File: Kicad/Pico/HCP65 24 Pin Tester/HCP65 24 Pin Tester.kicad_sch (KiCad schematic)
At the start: 64 parts, among them IC1 SN74ABT245BDBR, IC2 SN74ABT245BDBR, IC3 SN74ABT245BDBR, J1 6339167-2, J3 Conn_01x12_Socket, J8 Conn_01x12_Socket, J9 Conn_01x12_Socket

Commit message: Added debug points to Tester boards.
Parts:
- added C10: 10μF, SamacSys_Parts:CP_Radial_D4.0mm_P2.00mm, symbol HCP65:C_Radial_D4.0mm_P2.00mm
- added H1, H2, H3, H4, H5, H6, H7, H8: MountingHole_Pad, MountingHole:MountingHole_3.2mm_M3_Pad, symbol Mechanical:MountingHole_Pad
- added LED49: 150224SS73100, SamacSys_Parts:150224SS73100A, symbol Wurth_Elektronik:150224SS73100
- added R12: 10KΩ, SamacSys_Parts:R_0805, symbol HCP65:R_0805
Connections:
- net 12V: now also H1.1
- net 5V_{1} renamed 5Vc
- net 5Vc: now also H4.1
- net 5V_{2} renamed 5Vb
- net 5Vb: now also H3.1
- net 5V_{3} renamed 5Va
- net 5Va: now also C10.1, H2.1, R12.1
- net GND_{1} renamed GNDd
- net GNDd: now also H8.1
- net GND_{2} renamed GNDc
- net GNDc: now also H6.1
- net GND_{3} renamed GNDb
- net GNDb: now also C10.2, H7.1, LED49.1
- net GND_{4} renamed GNDa
- net GNDa: now also H5.1
- new net: LED49.2, R12.2
- no-connect marks 7 -> 5

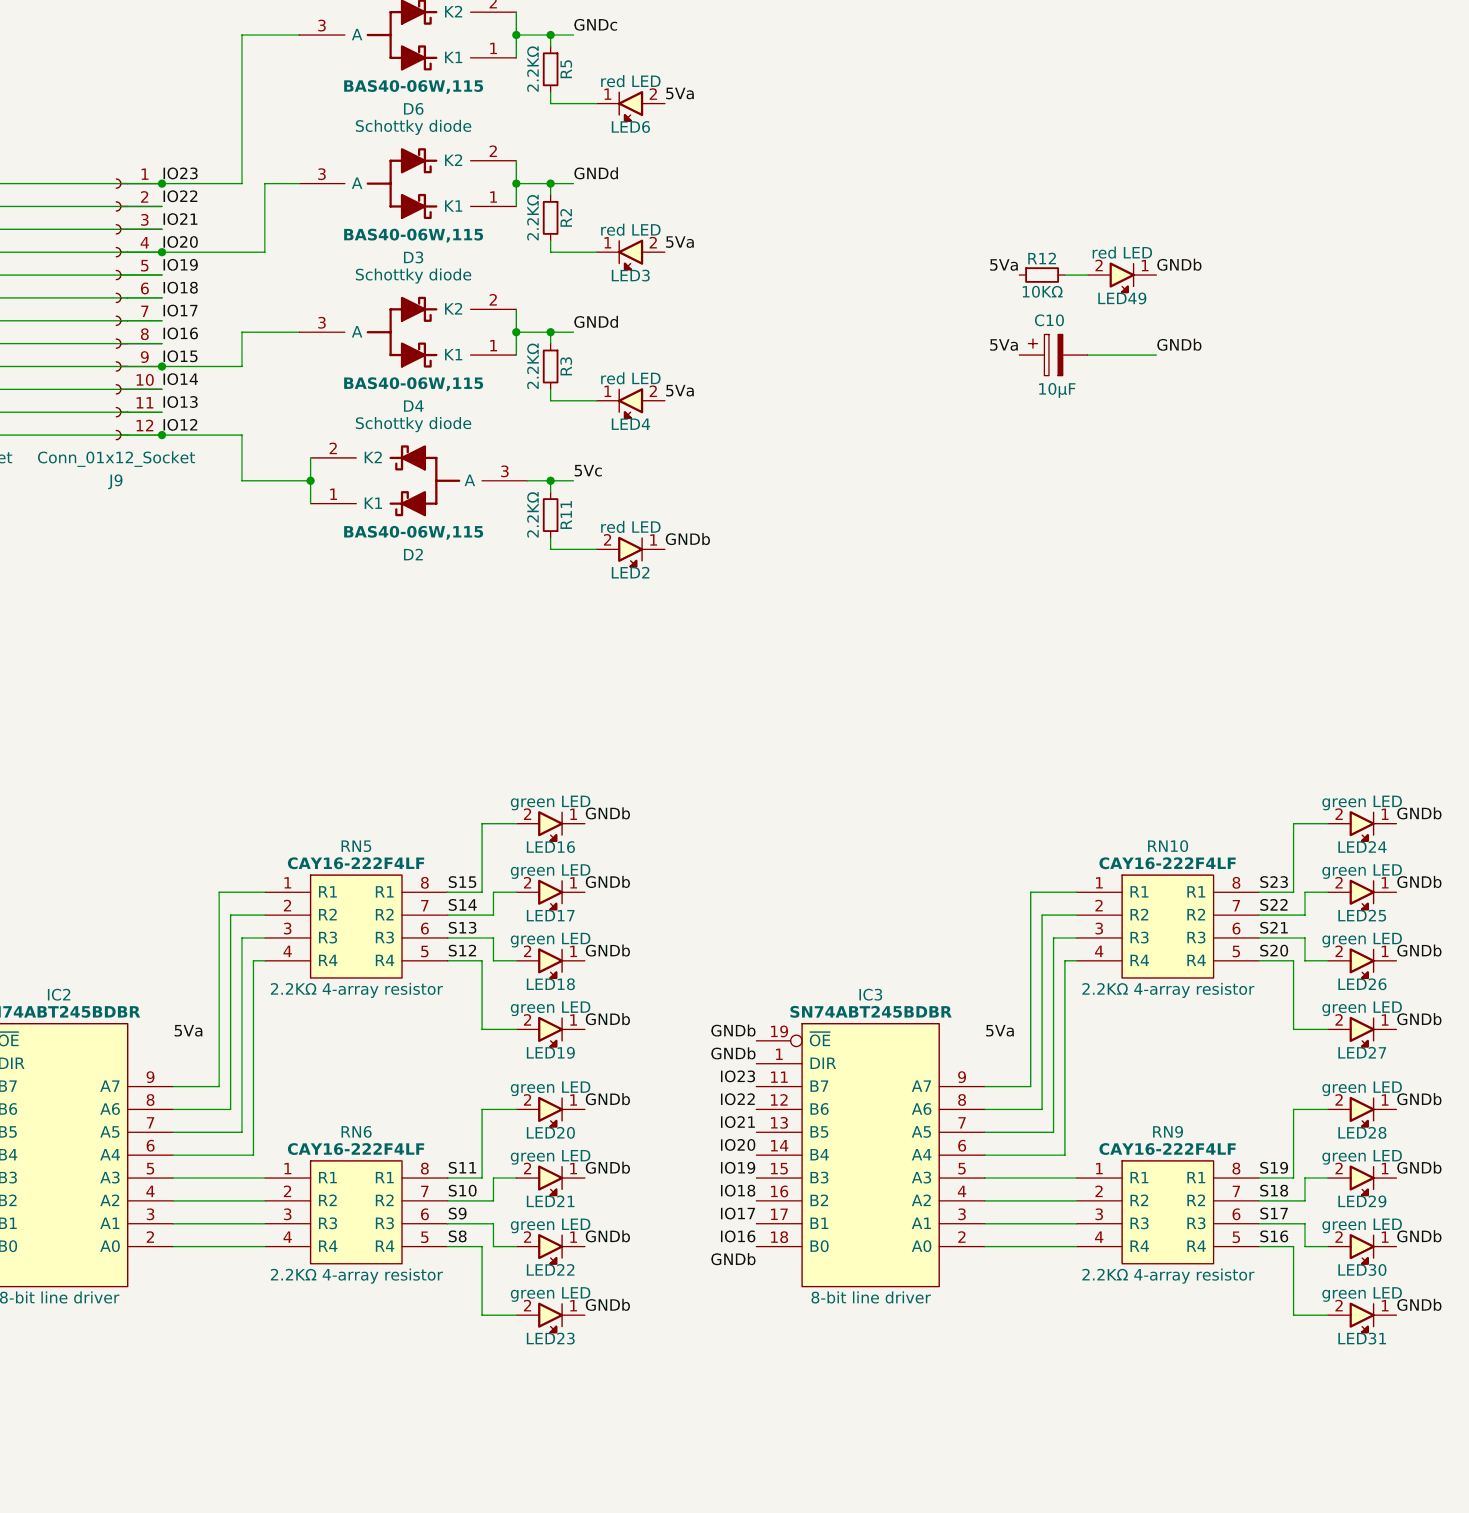
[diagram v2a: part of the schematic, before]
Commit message: Started fixing 24, 32 and 40 pin Tester Boards.
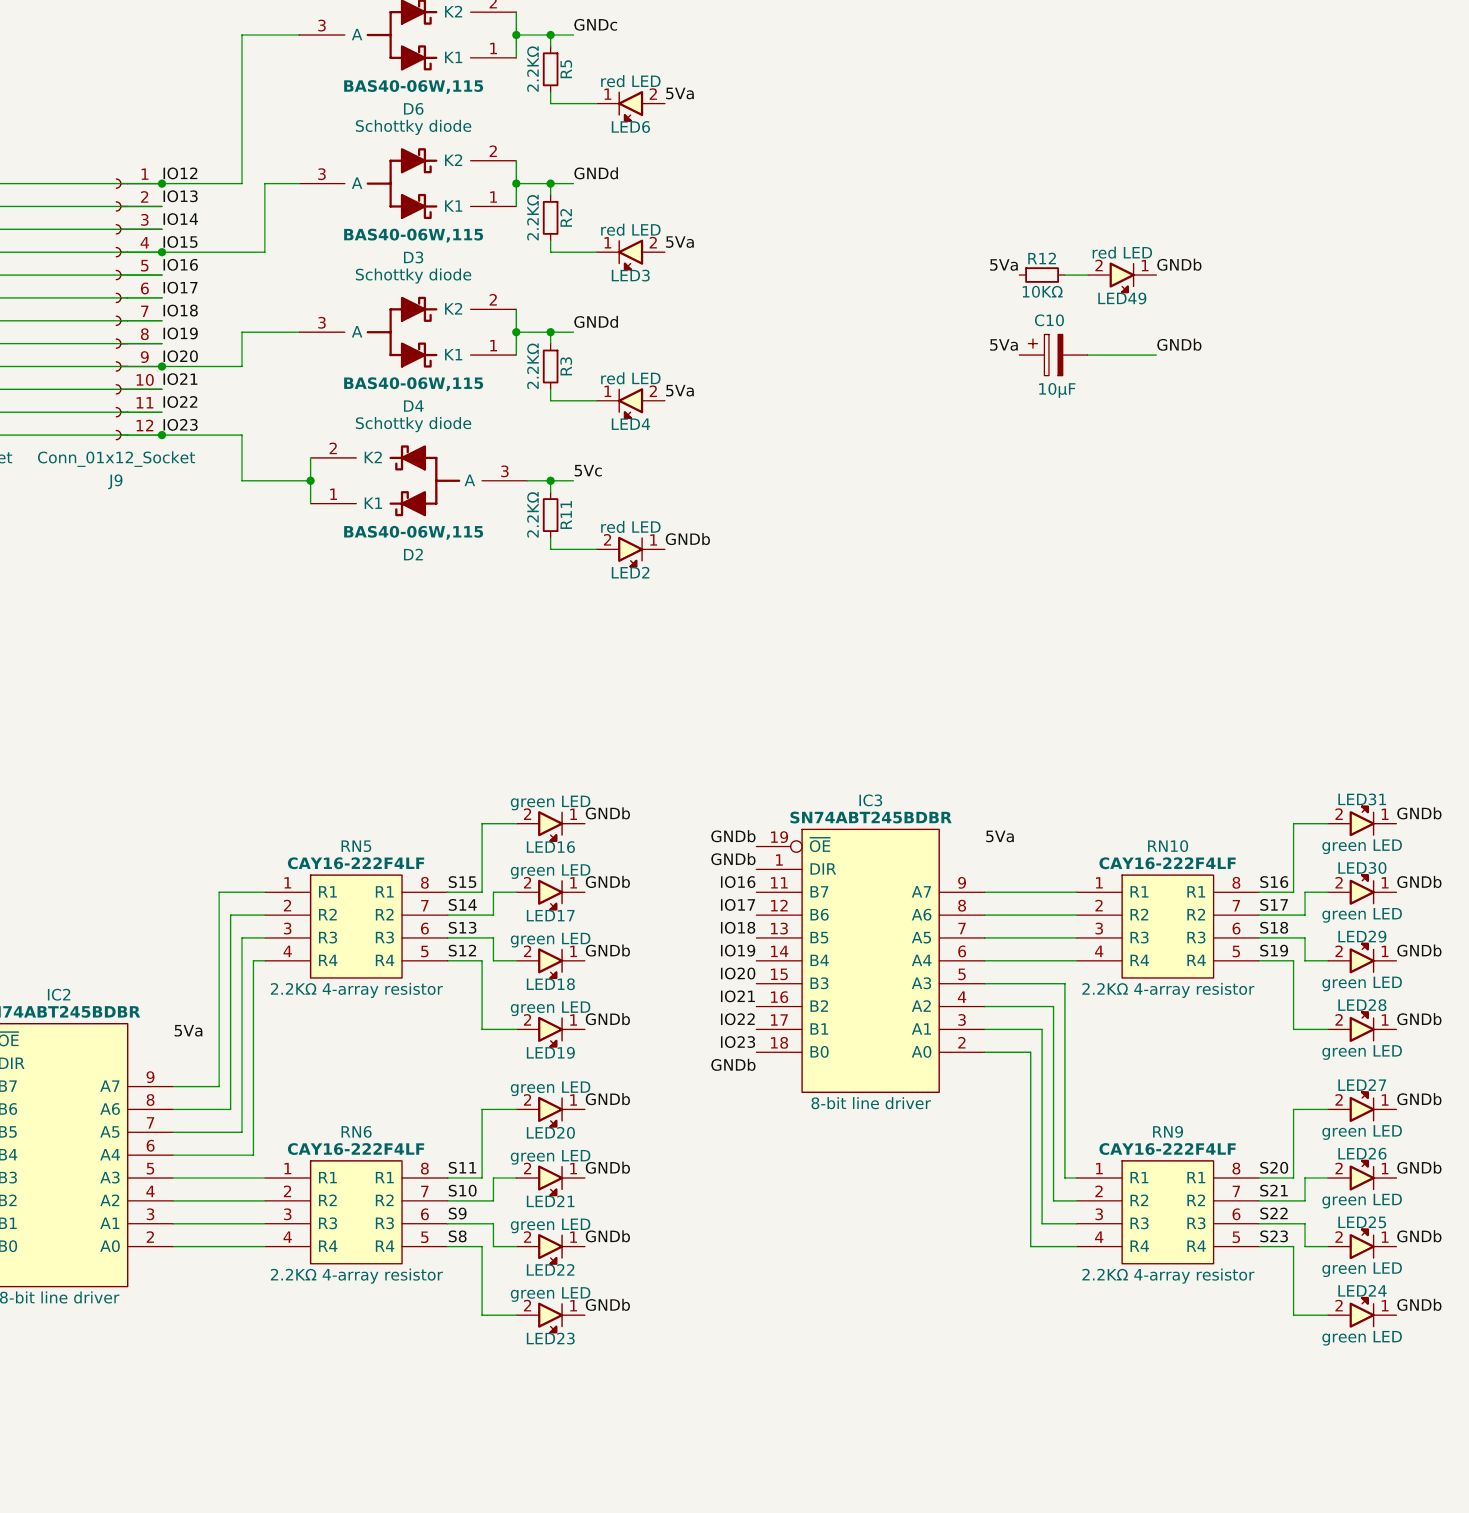
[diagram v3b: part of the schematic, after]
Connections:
- net IO12: now also D6.3 (A), J3.1 (Pin_1), J9.1 (Pin_1); no longer D2.1 (K1), D2.2 (K2), J3.12 (Pin_12), J9.12 (Pin_12)
- net IO13: now also J3.2 (Pin_2), J9.2 (Pin_2); no longer J3.11 (Pin_11), J9.11 (Pin_11)
- net IO14: now also J3.3 (Pin_3), J9.3 (Pin_3); no longer J3.10 (Pin_10), J9.10 (Pin_10)
- net IO15: now also D3.3 (A), J3.4 (Pin_4), J9.4 (Pin_4); no longer D4.3 (A), J3.9 (Pin_9), J9.9 (Pin_9)
- net IO16: now also IC3.11 (B7), J3.5 (Pin_5), J9.5 (Pin_5); no longer IC3.18 (B0), J3.8 (Pin_8), J9.8 (Pin_8)
- net IO17: now also IC3.12 (B6), J3.6 (Pin_6), J9.6 (Pin_6); no longer IC3.17 (B1), J3.7 (Pin_7), J9.7 (Pin_7)
- net IO18: now also IC3.13 (B5), J3.7 (Pin_7), J9.7 (Pin_7); no longer IC3.16 (B2), J3.6 (Pin_6), J9.6 (Pin_6)
- net IO19: now also IC3.14 (B4), J3.8 (Pin_8), J9.8 (Pin_8); no longer IC3.15 (B3), J3.5 (Pin_5), J9.5 (Pin_5)
- net IO20: now also D4.3 (A), IC3.15 (B3), J3.9 (Pin_9), J9.9 (Pin_9); no longer D3.3 (A), IC3.14 (B4), J3.4 (Pin_4), J9.4 (Pin_4)
- net IO21: now also IC3.16 (B2), J3.10 (Pin_10), J9.10 (Pin_10); no longer IC3.13 (B5), J3.3 (Pin_3), J9.3 (Pin_3)
- net IO22: now also IC3.17 (B1), J3.11 (Pin_11), J9.11 (Pin_11); no longer IC3.12 (B6), J3.2 (Pin_2), J9.2 (Pin_2)
- net IO23: now also D2.1 (K1), D2.2 (K2), IC3.18 (B0), J3.12 (Pin_12), J9.12 (Pin_12); no longer D6.3 (A), IC3.11 (B7), J3.1 (Pin_1), J9.1 (Pin_1)
- net S16: now also RN10.8 (R1); no longer RN9.5 (R4)
- net S17: now also RN10.7 (R2); no longer RN9.6 (R3)
- net S18: now also RN10.6 (R3); no longer RN9.7 (R2)
- net S19: now also RN10.5 (R4); no longer RN9.8 (R1)
- net S20: now also RN9.8 (R1); no longer RN10.5 (R4)
- net S21: now also RN9.7 (R2); no longer RN10.6 (R3)
- net S22: now also RN9.6 (R3); no longer RN10.7 (R2)
- net S23: now also RN9.5 (R4); no longer RN10.8 (R1)
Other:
- moved on the sheet: IC3, LED24, LED25, LED26, LED27, LED28, LED29, LED30, LED31

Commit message: Generate Tester Gerbers for V2 fabrication.
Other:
- moved on the sheet: H1, H2, H3, H4, H5, H6, H7, H8
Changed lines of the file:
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@@
 	)
 	(label "GNDc"
-		(at 38.1 273.05 270)
+		(at 39.37 194.31 270)
 		(effects
 			(font
@@
 	)
 	(label "GNDa"
-		(at 38.1 257.81 270)
+		(at 39.37 179.07 270)
 		(effects
 			(font
@@
 	)
 	(label "12V"
-		(at 38.1 227.33 270)
+		(at 39.37 148.59 270)
 		(effects
 			(font
@@
 	)
 	(label "GNDb"
-		(at 57.15 257.81 270)
+		(at 58.42 179.07 270)
 		(effects
 			(font
@@
 	)
 	(label "GNDd"
-		(at 57.15 273.05 270)
+		(at 58.42 194.31 270)
 		(effects
 			(font
@@
 	)
 	(label "5Vc"
-		(at 57.15 242.57 270)
+		(at 58.42 163.83 270)
 		(effects
 			(font
@@
 	)
 	(label "5Vb"
-		(at 38.1 242.57 270)
+		(at 39.37 163.83 270)
 		(effects
 			(font
@@
 	)
 	(label "5Va"
-		(at 57.15 227.33 270)
+		(at 58.42 148.59 270)
 		(effects
 			(font
@@
 	(symbol
 		(lib_id "Mechanical:MountingHole_Pad")
-		(at 57.15 240.03 0)
+		(at 58.42 161.29 0)
 		(unit 1)
 		(exclude_from_sim no)
@@
 		(dnp no)
 		(property "Reference" "H4"
-			(at 57.15 233.68 0)
+			(at 58.42 154.94 0)
 			(effects
 				(font
@@
 		)
 		(property "Value" "MountingHole_Pad"
-			(at 57.15 235.585 0)
+			(at 58.42 156.845 0)
 			(effects
 				(font
@@
 		)
 		(property "Footprint" "MountingHole:MountingHole_3.2mm_M3_Pad"
-			(at 57.15 240.03 0)
+			(at 58.42 161.29 0)
 			(effects
 				(font
@@
 		)
 		(property "Datasheet" "~"
-			(at 57.15 240.03 0)
+			(at 58.42 161.29 0)
 			(effects
 				(font
@@
 		)
 		(property "Description" "Mounting Hole with connection"
-			(at 57.15 240.03 0)
+			(at 58.42 161.29 0)
 			(effects
 				(font
@@
 	(symbol
 		(lib_id "Mechanical:MountingHole_Pad")
-		(at 57.15 270.51 0)
+		(at 58.42 191.77 0)
 		(unit 1)
 		(exclude_from_sim no)
@@
 		(dnp no)
 		(property "Reference" "H8"
-			(at 57.15 264.16 0)
+			(at 58.42 185.42 0)
 			(effects
 				(font
@@
 		)
 		(property "Value" "MountingHole_Pad"
-			(at 57.15 266.065 0)
+			(at 58.42 187.325 0)
 			(effects
 				(font
@@
 		)
 		(property "Footprint" "MountingHole:MountingHole_3.2mm_M3_Pad"
-			(at 57.15 270.51 0)
+			(at 58.42 191.77 0)
 			(effects
 				(font
@@
 		)
 		(property "Datasheet" "~"
-			(at 57.15 270.51 0)
+			(at 58.42 191.77 0)
 			(effects
 				(font
@@
 		)
 		(property "Description" "Mounting Hole with connection"
-			(at 57.15 270.51 0)
+			(at 58.42 191.77 0)
 			(effects
 				(font
@@
 	(symbol
 		(lib_id "Mechanical:MountingHole_Pad")
-		(at 38.1 270.51 0)
+		(at 39.37 191.77 0)
 		(unit 1)
 		(exclude_from_sim no)
@@
 		(dnp no)
 		(property "Reference" "H6"
-			(at 38.1 264.16 0)
+			(at 39.37 185.42 0)
 			(effects
 				(font
@@
 		)
 		(property "Value" "MountingHole_Pad"
-			(at 38.1 266.065 0)
+			(at 39.37 187.325 0)
 			(effects
 				(font
@@
 		)
 		(property "Footprint" "MountingHole:MountingHole_3.2mm_M3_Pad"
-			(at 38.1 270.51 0)
+			(at 39.37 191.77 0)
 			(effects
 				(font
@@
 		)
 		(property "Datasheet" "~"
-			(at 38.1 270.51 0)
+			(at 39.37 191.77 0)
 			(effects
 				(font
@@
 		)
 		(property "Description" "Mounting Hole with connection"
-			(at 38.1 270.51 0)
+			(at 39.37 191.77 0)
 			(effects
 				(font
@@
 	(symbol
 		(lib_id "Mechanical:MountingHole_Pad")
-		(at 57.15 255.27 0)
+		(at 58.42 176.53 0)
 		(unit 1)
 		(exclude_from_sim no)
@@
 		(dnp no)
 		(property "Reference" "H7"
-			(at 57.15 248.92 0)
+			(at 58.42 170.18 0)
 			(effects
 				(font
@@
 		)
 		(property "Value" "MountingHole_Pad"
-			(at 57.15 250.825 0)
+			(at 58.42 172.085 0)
 			(effects
 				(font
@@
 		)
 		(property "Footprint" "MountingHole:MountingHole_3.2mm_M3_Pad"
-			(at 57.15 255.27 0)
+			(at 58.42 176.53 0)
 			(effects
 				(font
@@
 		)
 		(property "Datasheet" "~"
-			(at 57.15 255.27 0)
+			(at 58.42 176.53 0)
 			(effects
 				(font
@@
 		)
 		(property "Description" "Mounting Hole with connection"
-			(at 57.15 255.27 0)
+			(at 58.42 176.53 0)
 			(effects
 				(font
@@
 	(symbol
 		(lib_id "Mechanical:MountingHole_Pad")
-		(at 38.1 255.27 0)
+		(at 39.37 176.53 0)
 		(unit 1)
 		(exclude_from_sim no)
@@
 		(dnp no)
 		(property "Reference" "H5"
-			(at 38.1 248.92 0)
+			(at 39.37 170.18 0)
 			(effects
 				(font
@@
 		)
 		(property "Value" "MountingHole_Pad"
-			(at 38.1 250.825 0)
+			(at 39.37 172.085 0)
 			(effects
 				(font
@@
 		)
 		(property "Footprint" "MountingHole:MountingHole_3.2mm_M3_Pad"
-			(at 38.1 255.27 0)
+			(at 39.37 176.53 0)
 			(effects
 				(font
@@
 		)
 		(property "Datasheet" "~"
-			(at 38.1 255.27 0)
+			(at 39.37 176.53 0)
 			(effects
 				(font
@@
 		)
 		(property "Description" "Mounting Hole with connection"
-			(at 38.1 255.27 0)
+			(at 39.37 176.53 0)
 			(effects
 				(font
@@
 	(symbol
 		(lib_id "Mechanical:MountingHole_Pad")
-		(at 38.1 240.03 0)
+		(at 39.37 161.29 0)
 		(unit 1)
 		(exclude_from_sim no)
@@
 		(dnp no)
 		(property "Reference" "H3"
-			(at 38.1 233.68 0)
+			(at 39.37 154.94 0)
 			(effects
 				(font
@@
 		)
 		(property "Value" "MountingHole_Pad"
-			(at 38.1 235.585 0)
+			(at 39.37 156.845 0)
 			(effects
 				(font
@@
 		)
 		(property "Footprint" "MountingHole:MountingHole_3.2mm_M3_Pad"
-			(at 38.1 240.03 0)
+			(at 39.37 161.29 0)
 			(effects
 				(font
@@
 		)
 		(property "Datasheet" "~"
-			(at 38.1 240.03 0)
+			(at 39.37 161.29 0)
 			(effects
 				(font
@@
 		)
 		(property "Description" "Mounting Hole with connection"
-			(at 38.1 240.03 0)
+			(at 39.37 161.29 0)
 			(effects
 				(font
@@
 	(symbol
 		(lib_id "Mechanical:MountingHole_Pad")
-		(at 38.1 224.79 0)
+		(at 39.37 146.05 0)
 		(unit 1)
 		(exclude_from_sim no)
@@
 		(dnp no)
 		(property "Reference" "H1"
-			(at 38.1 218.44 0)
+			(at 39.37 139.7 0)
 			(effects
 				(font
@@
 		)
 		(property "Value" "MountingHole_Pad"
-			(at 38.1 220.345 0)
+			(at 39.37 141.605 0)
 			(effects
 				(font
@@
 		)
 		(property "Footprint" "MountingHole:MountingHole_3.2mm_M3_Pad"
-			(at 38.1 224.79 0)
+			(at 39.37 146.05 0)
 			(effects
 				(font
@@
 		)
 		(property "Datasheet" "~"
-			(at 38.1 224.79 0)
+			(at 39.37 146.05 0)
 			(effects
 				(font
@@
 		)
 		(property "Description" "Mounting Hole with connection"
-			(at 38.1 224.79 0)
+			(at 39.37 146.05 0)
 			(effects
 				(font
@@
 	(symbol
 		(lib_id "Mechanical:MountingHole_Pad")
-		(at 57.15 224.79 0)
+		(at 58.42 146.05 0)
 		(unit 1)
 		(exclude_from_sim no)
@@
 		(dnp no)
 		(property "Reference" "H2"
-			(at 57.15 218.44 0)
+			(at 58.42 139.7 0)
 			(effects
 				(font
@@
 		)
 		(property "Value" "MountingHole_Pad"
-			(at 57.15 220.345 0)
+			(at 58.42 141.605 0)
 			(effects
 				(font
@@
 		)
 		(property "Footprint" "MountingHole:MountingHole_3.2mm_M3_Pad"
-			(at 57.15 224.79 0)
+			(at 58.42 146.05 0)
 			(effects
 				(font
@@
 		)
 		(property "Datasheet" "~"
-			(at 57.15 224.79 0)
+			(at 58.42 146.05 0)
 			(effects
 				(font
@@
 		)
 		(property "Description" "Mounting Hole with connection"
-			(at 57.15 224.79 0)
+			(at 58.42 146.05 0)
 			(effects
 				(font
